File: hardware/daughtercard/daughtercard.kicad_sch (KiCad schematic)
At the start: 48 parts, among them J1 Anzeige, J2 Bus in, J3 Bus out, J4 42V~ in, J5 42V~ out, J6 UPDI, Q1 BSS84, Q2 MMBT3904, Q3 MMBT3904, U1 ATtiny1616-SNR, U2 TP8485E-SR

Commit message: T4: PNG-Schaltplanvorschau + Bauteile nach Funktionsblöcken gruppiert
- gen_daughtercard_sch.py --png schreibt docs/daughtercard.png: eigener
  PDF-Export ohne Rahmen, zu PNG gerendert (pdftoppm) und auf den Inhalt
  zugeschnitten (Pillow). Fuer den schnellen optischen Check direkt auf GitHub,
  eingebunden in hardware/daughtercard/README.md.
- Bauteile werden jetzt blockweise mit Titel platziert (MCU, RS-485-Bus,
  Versorgung, Triac, 3x Impulseingang, CHAIN, Status/UPDI, Stecker, Testpunkte)
  statt in einem reinen Index-Raster. ERC weiter 0/0.
- setup.sh: poppler-utils und pillow ergaenzt (fuer --png).

Co-Authored-By: Claude Sonnet 5 <noreply@anthropic.com>
Claude-Session: https://claude.ai/code/session_01UsXTvE3jGgoK5Hec7hVbyD
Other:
- note added: "CHAIN / Enumeration"
- note added: "Impulseingang Blatt (PA4)"
- note added: "Impulseingang Leerbild (PA5)"
- note added: "Impulseingang Nullimpuls (PA6)"
- note added: "MCU"
- note added: "RS-485-Bus"
- note added: "Status-LED / UPDI"
- note added: "Stecker"
- note added: "Testpunkte"
- note added: "Triac-Ansteuerung"
- note added: "Versorgung"

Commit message: T5: Footprints zugeordnet, PCB-Netzliste exportierbar, Platzierungsvorschlag
- gen_daughtercard_sch.py: FOOTPRINTS deckt alle 48 Bauteile ab. Grundlage
  schaltplan-daughtercard.md Kap. 1/3/5 (Passive 0805; R14 und R16 in 1206,
  C3 1206; SOIC-20W/300mil fuer U1; SOT-23; IDC-Wannenstecker 2x5; Phoenix-
  Schraubklemme 5,08 mm; SolderJumper 2-Pad; Testpad D1,5 mm). Der Konsistenz-
  check prueft jetzt zusaetzlich, dass jeder Footprint in der KiCad-
  Footprintbibliothek existiert.
- --netlist exportiert hardware/daughtercard/daughtercard.net (kicadsexpr,
  .gitignore). 48 Bauteile, 40 Netze, jedes Bauteil mit Footprint -> im
  PCB-Editor importierbar.
- docs/layout-daughtercard.md: Platzierungsvorschlag nach Schaltplan Kap. 8
  (AC-Zone Unterkante, Logik Mitte, Bus oben; Leiterbahn- und Abstandsvorgaben;
  Checkliste vor dem Routen).
- P-1/P-2 in docs/pruefpunkte-t4.md als freigegeben eingetragen (Betreiber, Chat).

ERC weiter 0 Fehler / 0 Warnungen. Das PCB-Layout selbst ist nicht Teil von T5.

Co-Authored-By: Claude Sonnet 5 <noreply@anthropic.com>
Claude-Session: https://claude.ai/code/session_01UsXTvE3jGgoK5Hec7hVbyD
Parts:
- C1, C2, C4, C5, C6: footprint (none) -> Capacitor_SMD:C_0805_2012Metric
- C3: footprint (none) -> Capacitor_SMD:C_1206_3216Metric
- D1, D2, D3, Q1, Q2, Q3: footprint (none) -> Package_TO_SOT_SMD:SOT-23
- D4: footprint (none) -> LED_SMD:LED_0805_2012Metric
- F1: footprint (none) -> Fuse:Fuse_1206_3216Metric
- J1, J2, J3: footprint (none) -> Connector_IDC:IDC-Header_2x05_P2.54mm_Vertical
- J4, J5: footprint (none) -> TerminalBlock_Phoenix:TerminalBlock_Phoenix_MKDS-1,5-2-5.08_1x02_P5.08mm_Horizontal
- J6: footprint (none) -> Connector_PinHeader_2.54mm:PinHeader_1x03_P2.54mm_Vertical
- JP1, JP2, JP3: footprint (none) -> Jumper:SolderJumper-2_P1.3mm_Open_Pad1.0x1.5mm
- R1, R10, R11, R12, R13, R15, R2, R3, R4, R5, R6, R7, R8, R9: footprint (none) -> Resistor_SMD:R_0805_2012Metric
- R14, R16: footprint (none) -> Resistor_SMD:R_1206_3216Metric
- TP1, TP2, TP3, TP4, TP5, TP6, TP7: footprint (none) -> TestPoint:TestPoint_Pad_D1.5mm
- U1: footprint (none) -> Package_SO:SOIC-20W_7.5x12.8mm_P1.27mm
- U2: footprint (none) -> Package_SO:SOIC-8_3.9x4.9mm_P1.27mm

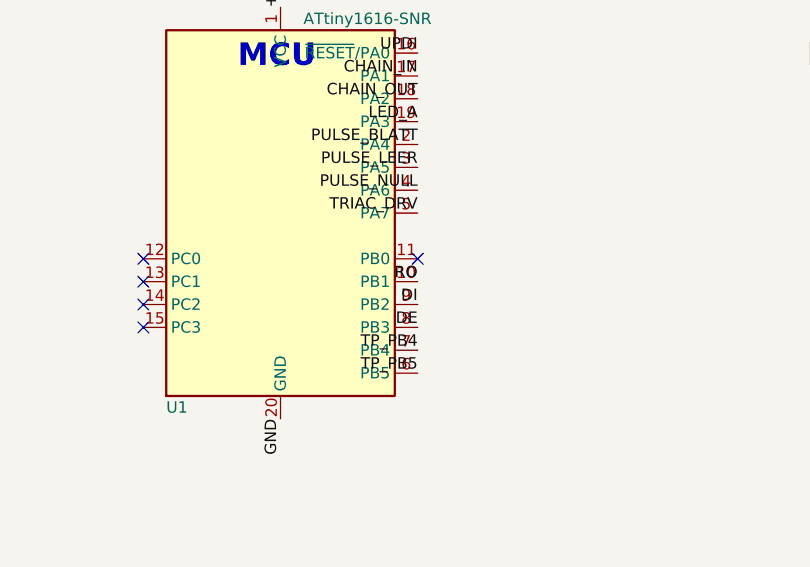
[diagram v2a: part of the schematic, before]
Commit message: T7 (P-3): RS-485 auf die USART0-Standardpins des ATtiny1616 korrigiert
Vom Betreiber freigegeben. RO an PB3 (Pin 8, war PB1), DE an PB0 (Pin 11, war
PB3), DI an PB2 (Pin 9) unveraendert. PB1 (Pin 10, USART0 XCK) wird neuer
unbeschalteter Reserve-Pin.

- tools/gen_daughtercard_sch.py: Netze RO/DE, NO_CONNECT_PINS (PB1 statt PB0).
  Schaltplan, PDF, PNG und Netzliste neu erzeugt. ERC weiter 0 Fehler / 0 Warnungen.
- docs/schaltplan-daughtercard.md v0.3 (5.2, 6.2, 6.3, Aenderungshistorie)
- docs/spezifikation.md v0.5 (4.2, Anhang D)
- docs/symbolpruefung.md: NL-Spalte in 2.1 nachgezogen (Datenblattpruefung unberuehrt)
- docs/pruefpunkte-t7.md: Freigabe eingetragen

Co-Authored-By: Claude Sonnet 5 <noreply@anthropic.com>
Claude-Session: https://claude.ai/code/session_01UsXTvE3jGgoK5Hec7hVbyD
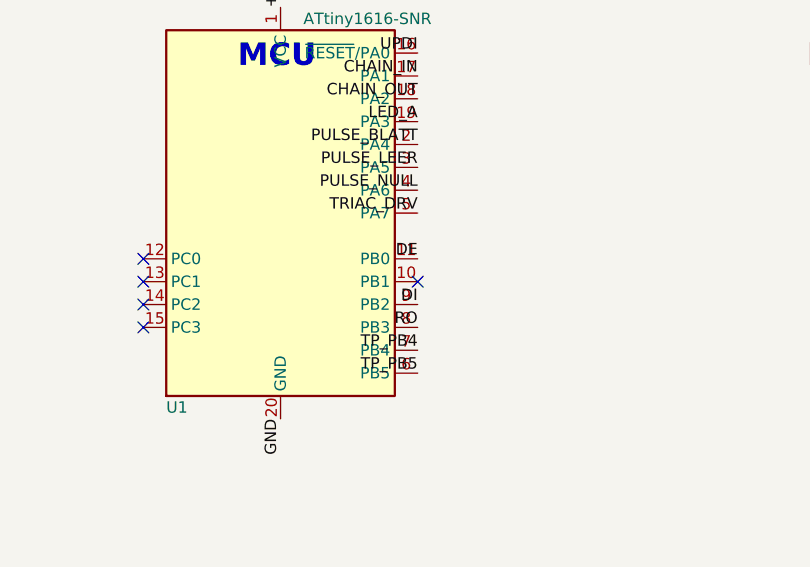
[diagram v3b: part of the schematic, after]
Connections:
- net DE: now also U1.11 (PB0); no longer U1.8 (PB3)
- net RO: now also U1.8 (PB3); no longer U1.10 (PB1)
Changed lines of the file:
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@@
 		(instances
 			(project "daughtercard"
-				(path "/b6504805-c0ef-475f-88ad-09b9eea28afc"
+				(path "/d4198d74-97df-4630-b0bf-d243d277f2c6"
 					(reference "U1")
 					(unit 1)
@@
 		(instances
 			(project "daughtercard"
-				(path "/b6504805-c0ef-475f-88ad-09b9eea28afc"
+				(path "/d4198d74-97df-4630-b0bf-d243d277f2c6"
 					(reference "U2")
 					(unit 1)
@@
 		(instances
 			(project "daughtercard"
-				(path "/b6504805-c0ef-475f-88ad-09b9eea28afc"
+				(path "/d4198d74-97df-4630-b0bf-d243d277f2c6"
 					(reference "R16")
 					(unit 1)
@@
 		(instances
 			(project "daughtercard"
-				(path "/b6504805-c0ef-475f-88ad-09b9eea28afc"
+				(path "/d4198d74-97df-4630-b0bf-d243d277f2c6"
 					(reference "JP3")
 					(unit 1)
@@
 		(instances
 			(project "daughtercard"
-				(path "/b6504805-c0ef-475f-88ad-09b9eea28afc"
+				(path "/d4198d74-97df-4630-b0bf-d243d277f2c6"
 					(reference "F1")
 					(unit 1)
@@
 		(instances
 			(project "daughtercard"
-				(path "/b6504805-c0ef-475f-88ad-09b9eea28afc"
+				(path "/d4198d74-97df-4630-b0bf-d243d277f2c6"
 					(reference "C1")
 					(unit 1)
@@
 		(instances
 			(project "daughtercard"
-				(path "/b6504805-c0ef-475f-88ad-09b9eea28afc"
+				(path "/d4198d74-97df-4630-b0bf-d243d277f2c6"
 					(reference "C2")
 					(unit 1)
@@
 		(instances
 			(project "daughtercard"
-				(path "/b6504805-c0ef-475f-88ad-09b9eea28afc"
+				(path "/d4198d74-97df-4630-b0bf-d243d277f2c6"
 					(reference "C3")
 					(unit 1)
@@
 		(instances
 			(project "daughtercard"
-				(path "/b6504805-c0ef-475f-88ad-09b9eea28afc"
+				(path "/d4198d74-97df-4630-b0bf-d243d277f2c6"
 					(reference "R14")
 					(unit 1)
@@
 		(instances
 			(project "daughtercard"
-				(path "/b6504805-c0ef-475f-88ad-09b9eea28afc"
+				(path "/d4198d74-97df-4630-b0bf-d243d277f2c6"
 					(reference "JP1")
 					(unit 1)
@@
 		(instances
 			(project "daughtercard"
-				(path "/b6504805-c0ef-475f-88ad-09b9eea28afc"
+				(path "/d4198d74-97df-4630-b0bf-d243d277f2c6"
 					(reference "JP2")
 					(unit 1)
@@
 		(instances
 			(project "daughtercard"
-				(path "/b6504805-c0ef-475f-88ad-09b9eea28afc"
+				(path "/d4198d74-97df-4630-b0bf-d243d277f2c6"
 					(reference "Q1")
 					(unit 1)
@@
 		(instances
 			(project "daughtercard"
-				(path "/b6504805-c0ef-475f-88ad-09b9eea28afc"
+				(path "/d4198d74-97df-4630-b0bf-d243d277f2c6"
 					(reference "Q2")
 					(unit 1)
@@
 		(instances
 			(project "daughtercard"
-				(path "/b6504805-c0ef-475f-88ad-09b9eea28afc"
+				(path "/d4198d74-97df-4630-b0bf-d243d277f2c6"
 					(reference "Q3")
 					(unit 1)
@@
 		(instances
 			(project "daughtercard"
-				(path "/b6504805-c0ef-475f-88ad-09b9eea28afc"
+				(path "/d4198d74-97df-4630-b0bf-d243d277f2c6"
 					(reference "R7")
 					(unit 1)
@@
 		(instances
 			(project "daughtercard"
-				(path "/b6504805-c0ef-475f-88ad-09b9eea28afc"
+				(path "/d4198d74-97df-4630-b0bf-d243d277f2c6"
 					(reference "R8")
 					(unit 1)
@@
 		(instances
 			(project "daughtercard"
-				(path "/b6504805-c0ef-475f-88ad-09b9eea28afc"
+				(path "/d4198d74-97df-4630-b0bf-d243d277f2c6"
 					(reference "R9")
 					(unit 1)
@@
 		(instances
 			(project "daughtercard"
-				(path "/b6504805-c0ef-475f-88ad-09b9eea28afc"
+				(path "/d4198d74-97df-4630-b0bf-d243d277f2c6"
 					(reference "R10")
 					(unit 1)
@@
 		(instances
 			(project "daughtercard"
-				(path "/b6504805-c0ef-475f-88ad-09b9eea28afc"
+				(path "/d4198d74-97df-4630-b0bf-d243d277f2c6"
 					(reference "R1")
 					(unit 1)
@@
 		(instances
 			(project "daughtercard"
-				(path "/b6504805-c0ef-475f-88ad-09b9eea28afc"
+				(path "/d4198d74-97df-4630-b0bf-d243d277f2c6"
 					(reference "R2")
 					(unit 1)
@@
 		(instances
 			(project "daughtercard"
-				(path "/b6504805-c0ef-475f-88ad-09b9eea28afc"
+				(path "/d4198d74-97df-4630-b0bf-d243d277f2c6"
 					(reference "C4")
 					(unit 1)
@@
 		(instances
 			(project "daughtercard"
-				(path "/b6504805-c0ef-475f-88ad-09b9eea28afc"
+				(path "/d4198d74-97df-4630-b0bf-d243d277f2c6"
 					(reference "D1")
 					(unit 1)
@@
 		(instances
 			(project "daughtercard"
-				(path "/b6504805-c0ef-475f-88ad-09b9eea28afc"
+				(path "/d4198d74-97df-4630-b0bf-d243d277f2c6"
 					(reference "R3")
 					(unit 1)
@@
 		(instances
 			(project "daughtercard"
-				(path "/b6504805-c0ef-475f-88ad-09b9eea28afc"
+				(path "/d4198d74-97df-4630-b0bf-d243d277f2c6"
 					(reference "R4")
 					(unit 1)
@@
 		(instances
 			(project "daughtercard"
-				(path "/b6504805-c0ef-475f-88ad-09b9eea28afc"
+				(path "/d4198d74-97df-4630-b0bf-d243d277f2c6"
 					(reference "C5")
 					(unit 1)
@@
 		(instances
 			(project "daughtercard"
-				(path "/b6504805-c0ef-475f-88ad-09b9eea28afc"
+				(path "/d4198d74-97df-4630-b0bf-d243d277f2c6"
 					(reference "D2")
 					(unit 1)
@@
 		(instances
 			(project "daughtercard"
-				(path "/b6504805-c0ef-475f-88ad-09b9eea28afc"
+				(path "/d4198d74-97df-4630-b0bf-d243d277f2c6"
 					(reference "R5")
 					(unit 1)
@@
 		(instances
 			(project "daughtercard"
-				(path "/b6504805-c0ef-475f-88ad-09b9eea28afc"
+				(path "/d4198d74-97df-4630-b0bf-d243d277f2c6"
 					(reference "R6")
 					(unit 1)
@@
 		(instances
 			(project "daughtercard"
-				(path "/b6504805-c0ef-475f-88ad-09b9eea28afc"
+				(path "/d4198d74-97df-4630-b0bf-d243d277f2c6"
 					(reference "C6")
 					(unit 1)
@@
 		(instances
 			(project "daughtercard"
-				(path "/b6504805-c0ef-475f-88ad-09b9eea28afc"
+				(path "/d4198d74-97df-4630-b0bf-d243d277f2c6"
 					(reference "D3")
 					(unit 1)
@@
 		(instances
 			(project "daughtercard"
-				(path "/b6504805-c0ef-475f-88ad-09b9eea28afc"
+				(path "/d4198d74-97df-4630-b0bf-d243d277f2c6"
 					(reference "R11")
 					(unit 1)
@@
 		(instances
 			(project "daughtercard"
-				(path "/b6504805-c0ef-475f-88ad-09b9eea28afc"
+				(path "/d4198d74-97df-4630-b0bf-d243d277f2c6"
 					(reference "R12")
 					(unit 1)
@@
 		(instances
 			(project "daughtercard"
-				(path "/b6504805-c0ef-475f-88ad-09b9eea28afc"
+				(path "/d4198d74-97df-4630-b0bf-d243d277f2c6"
 					(reference "R13")
 					(unit 1)
@@
 		(instances
 			(project "daughtercard"
-				(path "/b6504805-c0ef-475f-88ad-09b9eea28afc"
+				(path "/d4198d74-97df-4630-b0bf-d243d277f2c6"
 					(reference "R15")
 					(unit 1)
@@
 		(instances
 			(project "daughtercard"
-				(path "/b6504805-c0ef-475f-88ad-09b9eea28afc"
+				(path "/d4198d74-97df-4630-b0bf-d243d277f2c6"
 					(reference "D4")
 					(unit 1)
@@
 		(instances
 			(project "daughtercard"
-				(path "/b6504805-c0ef-475f-88ad-09b9eea28afc"
+				(path "/d4198d74-97df-4630-b0bf-d243d277f2c6"
 					(reference "J6")
 					(unit 1)
@@
 		(instances
 			(project "daughtercard"
-				(path "/b6504805-c0ef-475f-88ad-09b9eea28afc"
+				(path "/d4198d74-97df-4630-b0bf-d243d277f2c6"
 					(reference "J1")
 					(unit 1)
@@
 		(instances
 			(project "daughtercard"
-				(path "/b6504805-c0ef-475f-88ad-09b9eea28afc"
+				(path "/d4198d74-97df-4630-b0bf-d243d277f2c6"
 					(reference "J2")
 					(unit 1)
@@
 		(instances
 			(project "daughtercard"
-				(path "/b6504805-c0ef-475f-88ad-09b9eea28afc"
+				(path "/d4198d74-97df-4630-b0bf-d243d277f2c6"
 					(reference "J3")
 					(unit 1)
@@
 		(instances
 			(project "daughtercard"
-				(path "/b6504805-c0ef-475f-88ad-09b9eea28afc"
+				(path "/d4198d74-97df-4630-b0bf-d243d277f2c6"
 					(reference "J4")
 					(unit 1)
@@
 		(instances
 			(project "daughtercard"
-				(path "/b6504805-c0ef-475f-88ad-09b9eea28afc"
+				(path "/d4198d74-97df-4630-b0bf-d243d277f2c6"
 					(reference "J5")
 					(unit 1)
@@
 		(instances
 			(project "daughtercard"
-				(path "/b6504805-c0ef-475f-88ad-09b9eea28afc"
+				(path "/d4198d74-97df-4630-b0bf-d243d277f2c6"
 					(reference "TP1")
 					(unit 1)
@@
 		(instances
 			(project "daughtercard"
-				(path "/b6504805-c0ef-475f-88ad-09b9eea28afc"
+				(path "/d4198d74-97df-4630-b0bf-d243d277f2c6"
 					(reference "TP2")
 					(unit 1)
@@
 		(instances
 			(project "daughtercard"
-				(path "/b6504805-c0ef-475f-88ad-09b9eea28afc"
+				(path "/d4198d74-97df-4630-b0bf-d243d277f2c6"
 					(reference "TP3")
 					(unit 1)
@@
 		(instances
 			(project "daughtercard"
-				(path "/b6504805-c0ef-475f-88ad-09b9eea28afc"
+				(path "/d4198d74-97df-4630-b0bf-d243d277f2c6"
 					(reference "TP4")
 					(unit 1)
@@
 		(instances
 			(project "daughtercard"
-				(path "/b6504805-c0ef-475f-88ad-09b9eea28afc"
+				(path "/d4198d74-97df-4630-b0bf-d243d277f2c6"
 					(reference "TP5")
 					(unit 1)
@@
 		(instances
 			(project "daughtercard"
-				(path "/b6504805-c0ef-475f-88ad-09b9eea28afc"
+				(path "/d4198d74-97df-4630-b0bf-d243d277f2c6"
 					(reference "TP6")
 					(unit 1)
@@
 		(instances
 			(project "daughtercard"
-				(path "/b6504805-c0ef-475f-88ad-09b9eea28afc"
+				(path "/d4198d74-97df-4630-b0bf-d243d277f2c6"
 					(reference "TP7")
 					(unit 1)
@@
 		(instances
 			(project "daughtercard"
-				(path "/b6504805-c0ef-475f-88ad-09b9eea28afc"
+				(path "/d4198d74-97df-4630-b0bf-d243d277f2c6"
 					(reference "#FLG1")
 					(unit 1)
@@
 		(instances
 			(project "daughtercard"
-				(path "/b6504805-c0ef-475f-88ad-09b9eea28afc"
+				(path "/d4198d74-97df-4630-b0bf-d243d277f2c6"
 					(reference "#FLG2")
 					(unit 1)
@@
 		(instances
 			(project "daughtercard"
-				(path "/b6504805-c0ef-475f-88ad-09b9eea28afc"
+				(path "/d4198d74-97df-4630-b0bf-d243d277f2c6"
 					(reference "#FLG3")
 					(unit 1)
@@
 		(instances
 			(project "daughtercard"
-				(path "/b6504805-c0ef-475f-88ad-09b9eea28afc"
+				(path "/d4198d74-97df-4630-b0bf-d243d277f2c6"
 					(reference "#FLG4")
 					(unit 1)
@@
 	)
 	(label "RO"
-		(at 40.64 46.99 0.0000)
+		(at 40.64 52.07 0.0000)
 		(effects
 			(font
@@
 	)
 	(label "DE"
-		(at 40.64 52.07 0.0000)
+		(at 40.64 44.45 0.0000)
 		(effects
 			(font
@@
 	)
 	(no_connect
-		(at 40.64 44.45)
+		(at 40.64 46.99)
 	)
 	(no_connect
